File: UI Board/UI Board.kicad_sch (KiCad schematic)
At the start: 7 parts, among them J1 XT60-M, J2 22035035, U1 UA78M05QDCYRG4Q1

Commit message: not much
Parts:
- RP1: footprint (none) -> SMV_Connectors:RP2040
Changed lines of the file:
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@@
 			)
 		)
-		(property "Footprint" ""
+		(property "Footprint" "SMV_Connectors:RP2040"
 			(at 212.344 88.646 0)
 			(effects

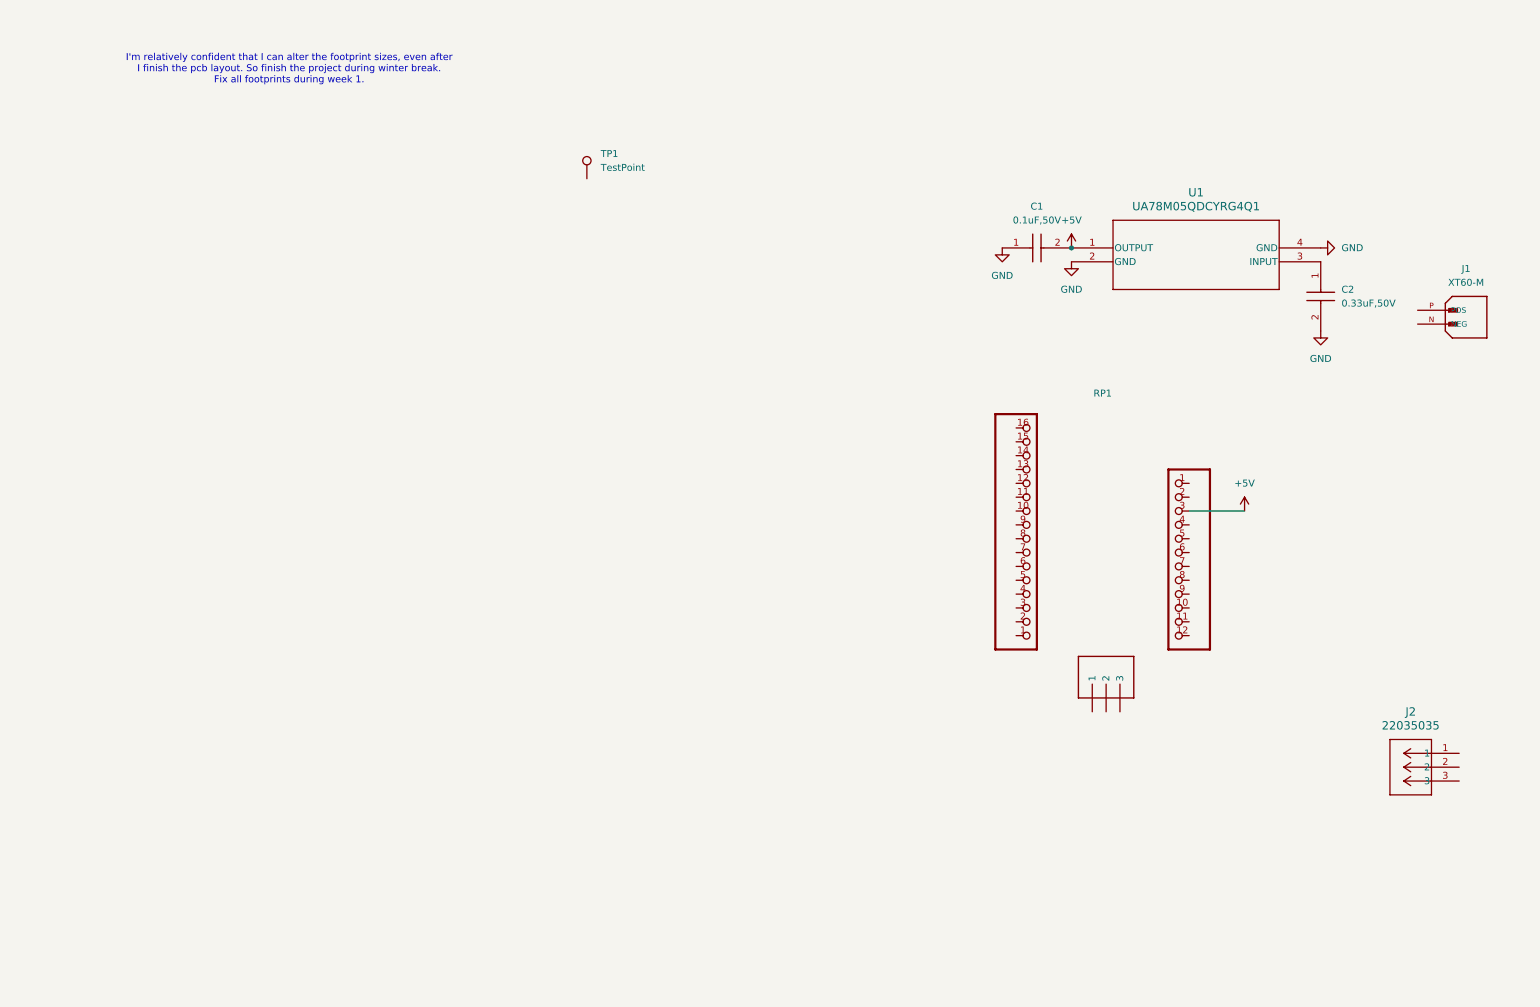
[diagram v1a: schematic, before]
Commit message: finished UI Board Schematic
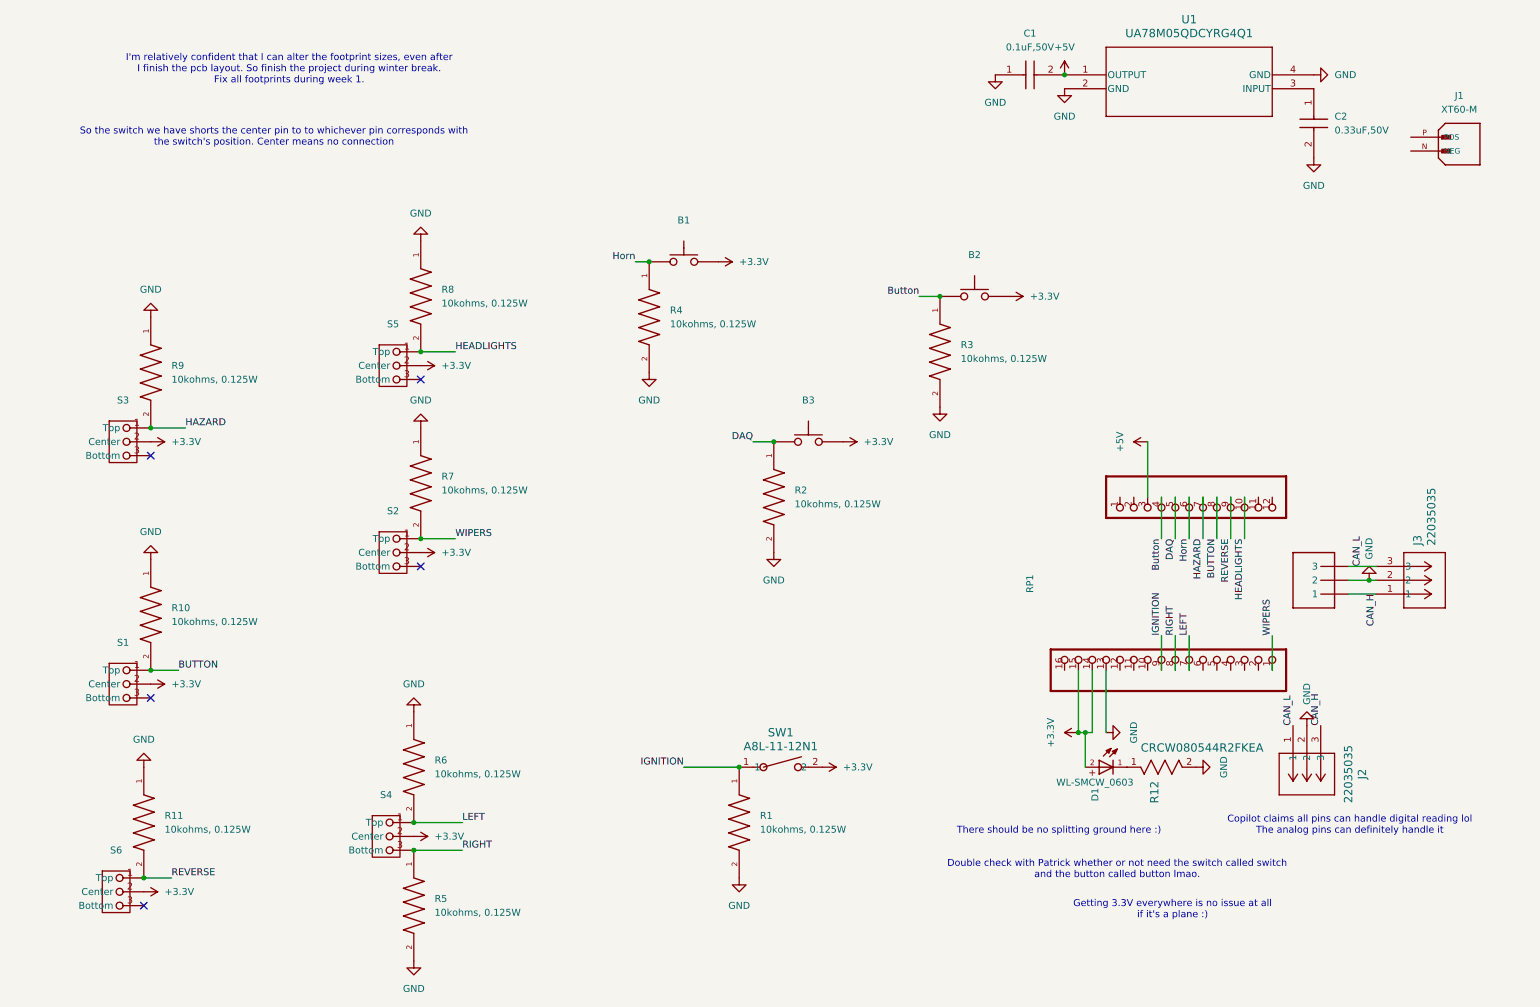
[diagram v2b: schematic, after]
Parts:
- removed TP1: TestPoint, symbol Connector:TestPoint
- added B1, B2, B3: ~, SMV_Misc:Twidec Button, symbol SMV_Custom:Twidec_Button
- added D1: WL-SMCW_0603, SMV_Passives:WL-SMCW_0603(diode), symbol SMV_Custom:WL-SMCW_0603
- added J3: 22035035, CON_22035035_MOL, symbol SMV_Custom:3-pin Mini Molex Spox
- added R1, R10, R11, R2, R3, R4, R5, R6, R7, R8, R9: 10kohms, 0.125W, SMV_Passives:0805RESC2012X60N, symbol SMV_Custom:CRCW080510K0FKEAC
- added R12: CRCW080544R2FKEA, SMV_Passives:0805RESC2012X60N, symbol SMV_Custom:CRCW080544R2FKEA
- added S1, S2, S3, S4, S5, S6: ~, SMV_Misc:TAISS 3 Pin Switch, symbol SMV_Custom:TAISS_3_Pin_Switch
- added SW1: A8L-11-12N1, SMV_Misc:SW_A8L-11_OMR, symbol SMV_Custom:A8L-11-12N1
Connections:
- net GND: now also J2.2, RP1.13, RP1.2, J3.2, R1.2, R10.1, R11.1, R12.2, R2.2, R3.2, R4.2, R5.2, R6.1, R7.1, R8.1, R9.1
- net WIPERS: now reaches RP1.1
- net WIPERS: now also R7.2, S2.1 (Top)
- net HEADLIGHTS: now reaches RP1.10
- net HEADLIGHTS: now also R8.2, S5.1 (Top)
- net +3.3V: now reaches RP1.14
- net +3.3V: now also RP1.15, B1., B2., B3., D1.2, S1.2 (Center), S2.2 (Center), S3.2 (Center), S4.2 (Center), S5.2 (Center), S6.2 (Center), SW1.2
- net CAN_L: now reaches RP1.3
- net CAN_L: now also J2.1, J3.3
- net Button: now reaches RP1.4
- net Button: now also B2., R3.1
- net DAQ: now reaches RP1.5
- net DAQ: now also B3., R2.1
- net Horn: now reaches RP1.6
- net Horn: now also B1., R4.1
- net LEFT: now reaches RP1.7
- net LEFT: now also R6.2, S4.1 (Top)
- net RIGHT: now reaches RP1.8
- net RIGHT: now also R5.1, S4.3 (Bottom)
- net REVERSE: now reaches RP1.9
- net REVERSE: now also R11.2, S6.1 (Top)
- net CAN_H: now reaches J2.3
- net CAN_H: now also RP1.1, J3.1
- new net: D1.1, R12.1
- new net BUTTON: R10.2, RP1.8, S1.1 (Top)
- new net HAZARD: R9.2, RP1.7, S3.1 (Top)
- new net IGNITION: R1.1, RP1.9, SW1.1
- no-connect marks 0 -> 5
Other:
- note added: "Copilot claims all pins can handle digital reading lol The analog pins can definitely handle it"
- note added: "Double check with Patrick whether or not need the switch called switch and the button called button lmao."
- note added: "Getting 3.3V everywhere is no issue at all if it's a plane :)"
- note added: "So the switch we have shorts the center pin to to whichever pin corresponds with the switch's position. Center means no connection"
- note added: "There should be no splitting ground here :)"
- moved on the sheet: C1, C2, J1, J2, RP1, U1

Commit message: UIBoardyay
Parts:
- J2, J3: footprint CON_22035035_MOL -> SMV_Connectors:3pin_CON_22035035_MOL
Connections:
- net +3.3V: now also B1.2, B2.2, B3.2, RP1.26 (3.3V), RP1.27 (3.3V); no longer B1., B2., B3., RP1.14, RP1.15
- net Button: now also B2.1; no longer B2.
- net CAN_H: now also RP1.31 (CAN_H); no longer RP1.1
- net CAN_L: now also RP1.29 (CAN_L); no longer RP1.3
- net DAQ: now also B3.1; no longer B3.
- net GND: now also J1.N (NEG), RP1.25 (GND), RP1.30 (GND); no longer RP1.13, RP1.2
- net Horn: now also B1.1; no longer B1.
- net IGNITION: now also RP1.21 (A3); no longer RP1.9
- net LEFT: now also RP1.19 (D25); no longer RP1.7
- net RIGHT: now also RP1.20 (D24); no longer RP1.8
- net WIPERS: now also RP1.13 (D4); no longer RP1.1
- net +12V: now reaches C2.1, U1.3 (INPUT)
- net +12V: now also J1.P (POS)
- net BUTTON renamed SWITCH
- no-connect marks 5 -> 18
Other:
- moved on the sheet: C1, C2, U1
